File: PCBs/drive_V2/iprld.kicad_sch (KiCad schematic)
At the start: 81 parts, among them IC1 W25Q16JVUXIQ_TR, IC2 ADS1115IDGSR, J1 TYPE-C-31-M-12, U1 AMS1117-3.3, U11 4N35, U12 4N35, U13 4N35, U14 4N35, U2 ESP32-S3, U3 4N35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

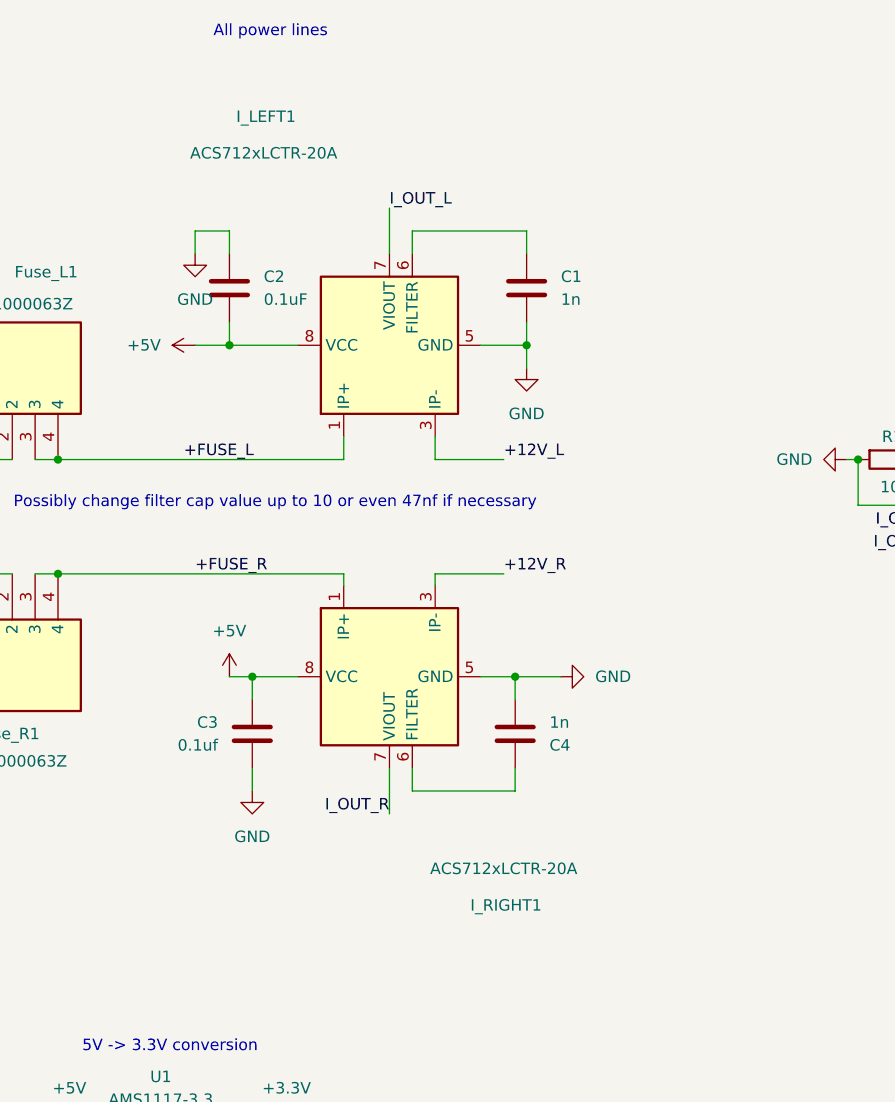
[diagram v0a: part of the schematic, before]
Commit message: added potential divider for I_OUT signals
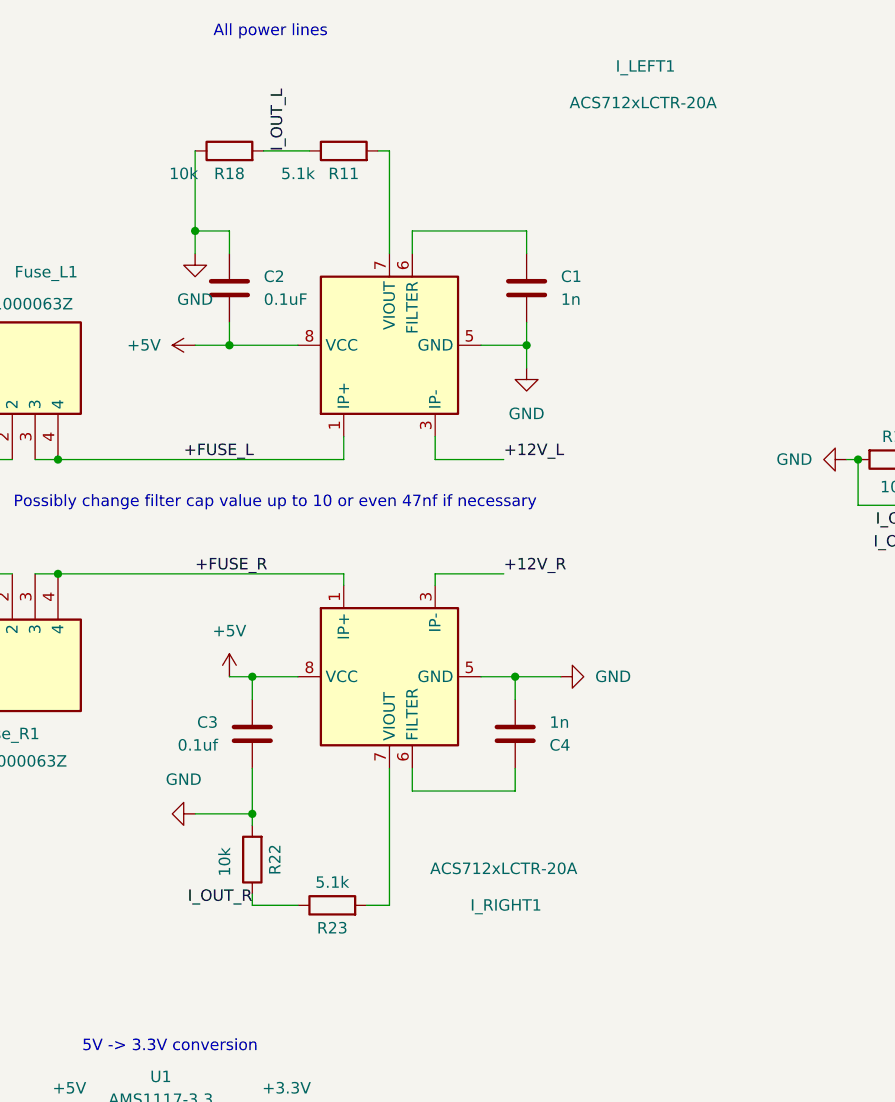
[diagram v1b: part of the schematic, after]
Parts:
- added R11, R23: 5.1k, Resistor_SMD:R_0805_2012Metric, symbol Device:R
- added R18, R22: 10k, Resistor_SMD:R_0805_2012Metric, symbol Device:R
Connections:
- net GND: now also R18.1, R22.2
- net I_OUT_L: now also R11.1, R18.2; no longer I_LEFT1.7 (VIOUT)
- net I_OUT_R: now also R22.1, R23.1; no longer I_RIGHT1.7 (VIOUT)
- new net: I_LEFT1.7 (VIOUT), R11.2
- new net: I_RIGHT1.7 (VIOUT), R23.2

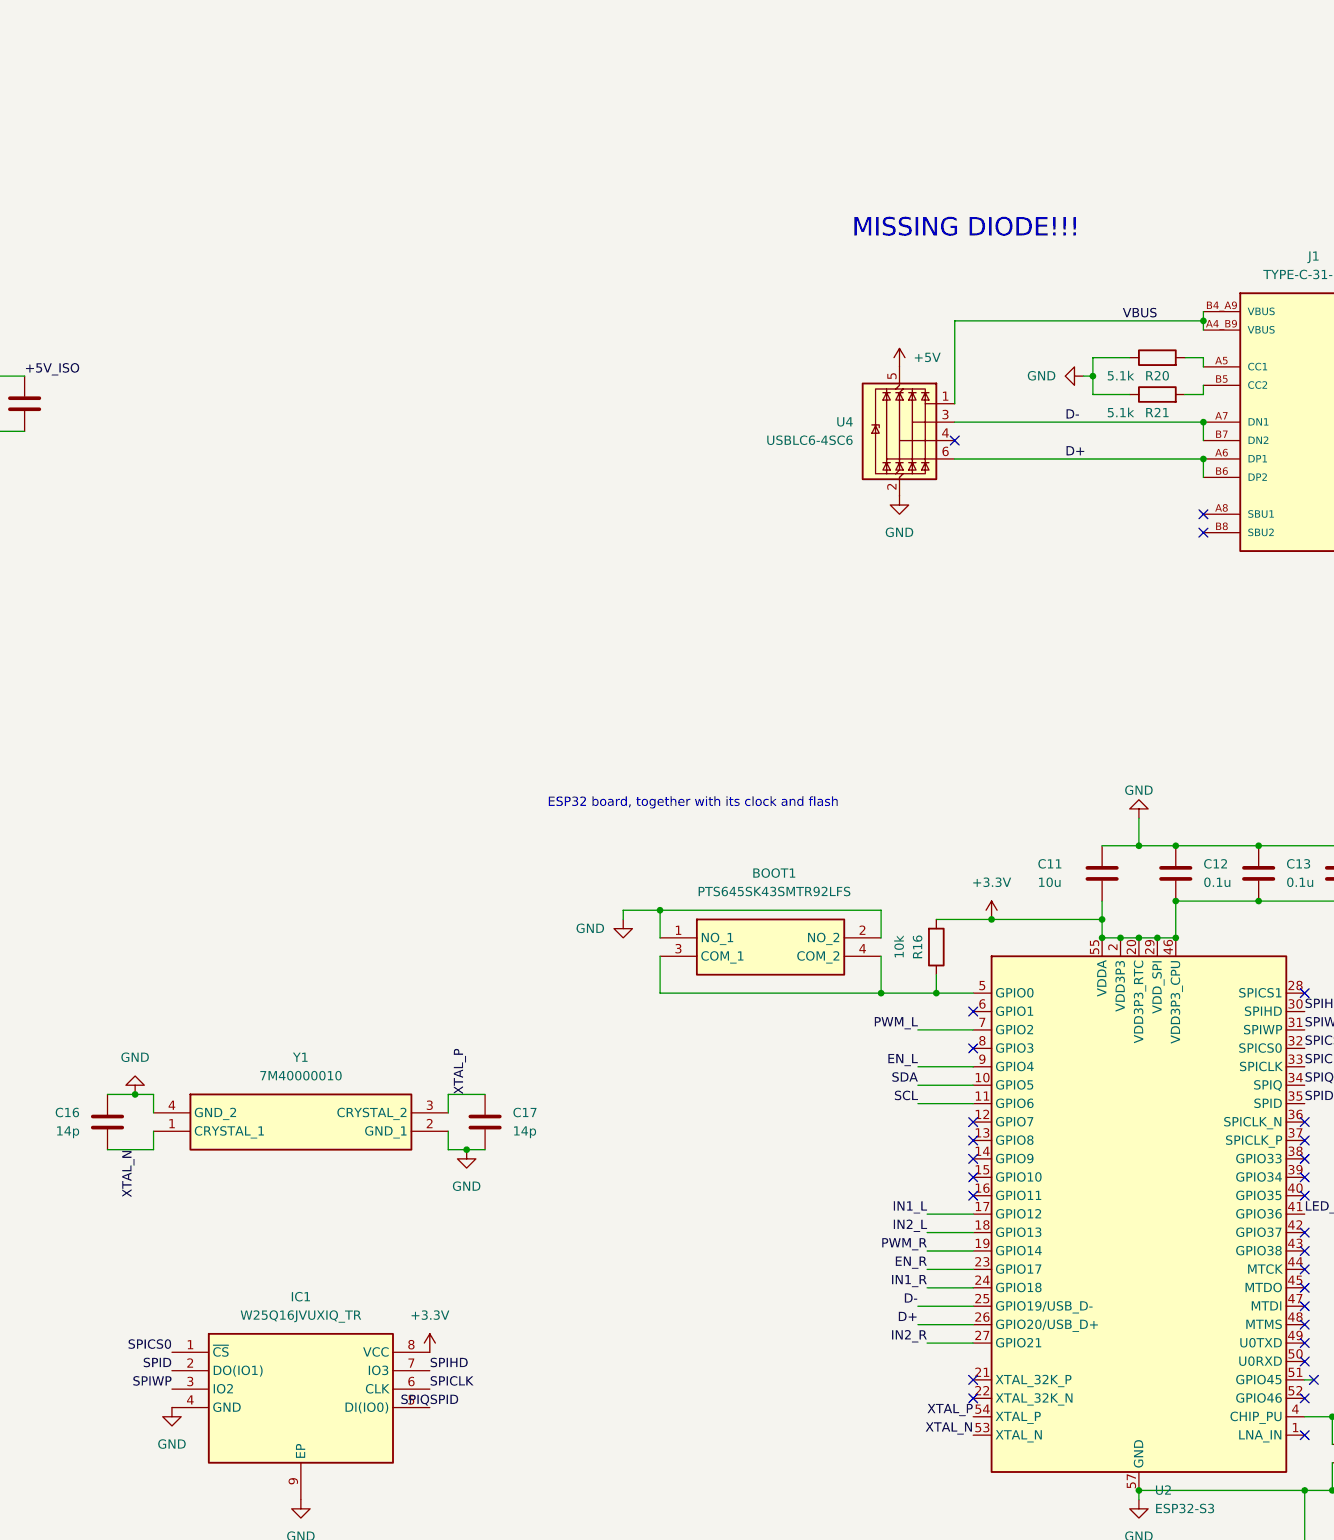
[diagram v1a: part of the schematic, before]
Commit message: readded Diode D1, fixed connection issue with SPID and SPIQ
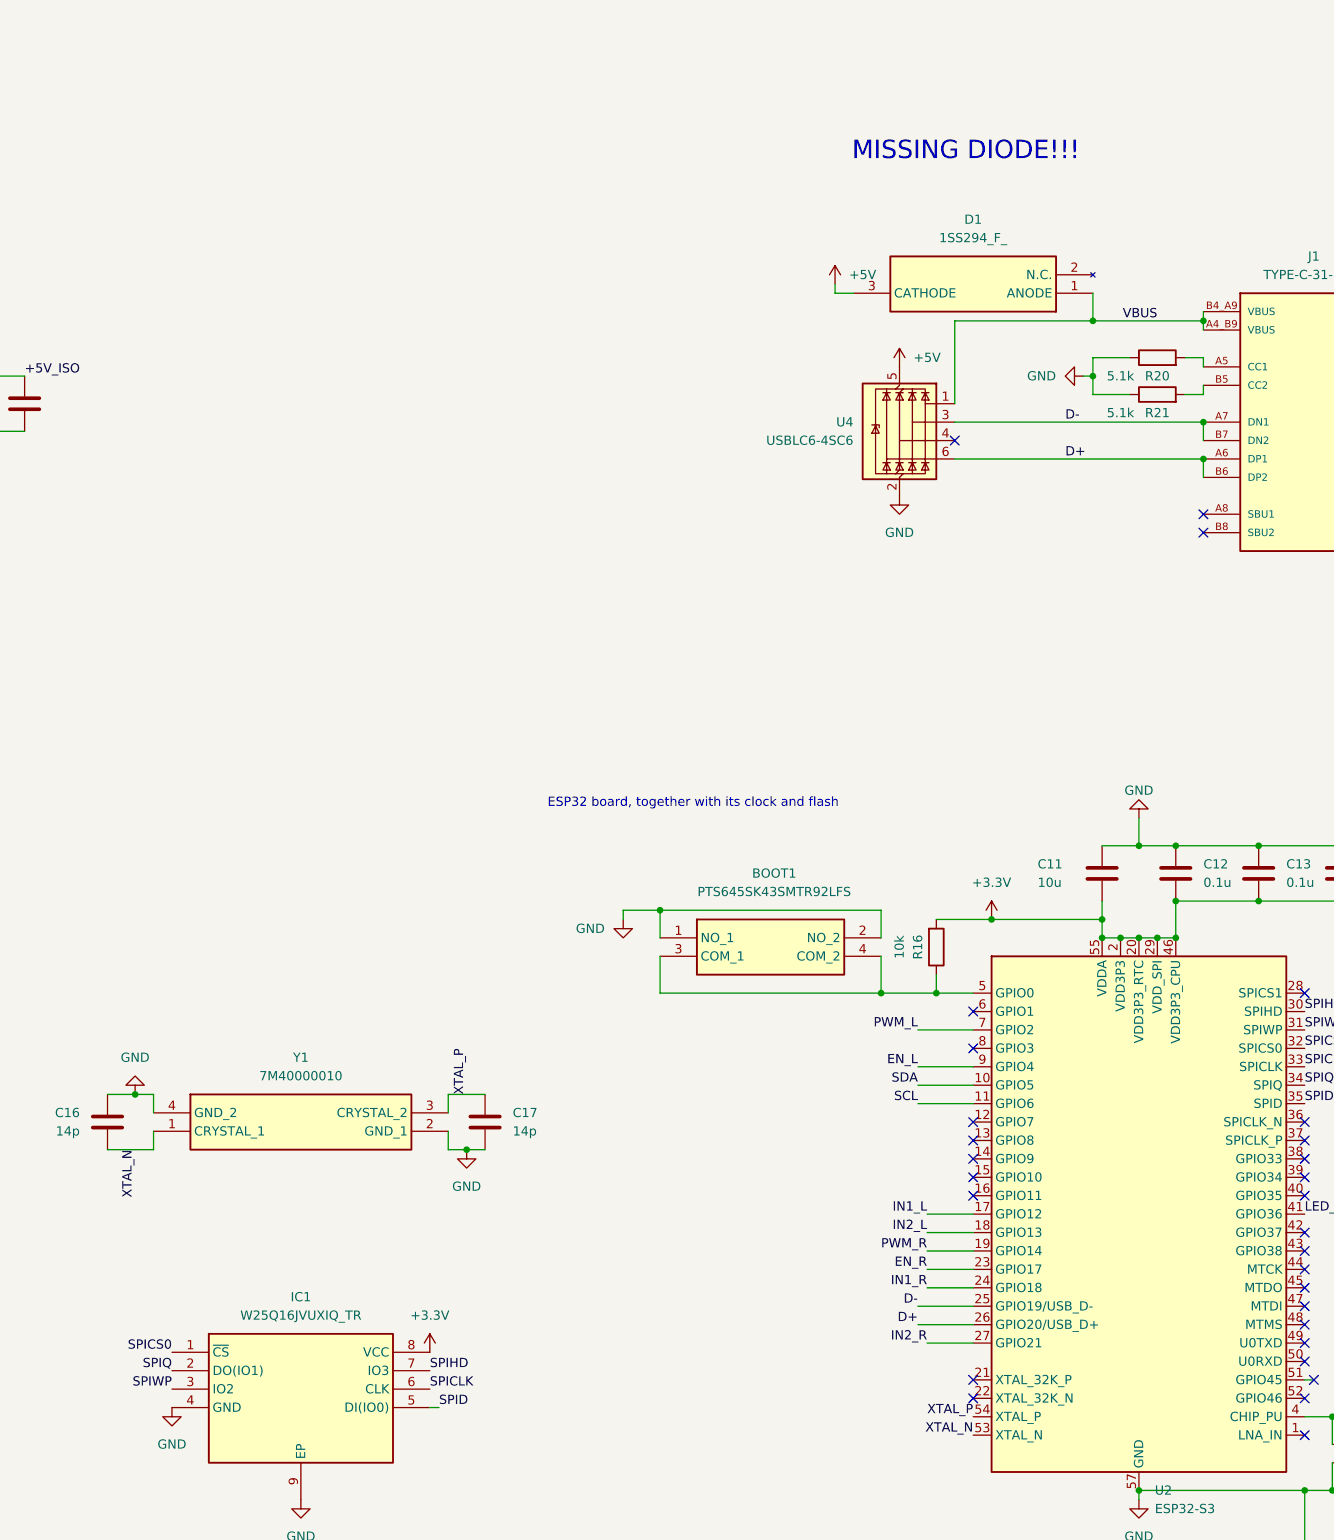
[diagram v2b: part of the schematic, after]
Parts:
- added D1: 1SS294_F_, iprl_footprint:SOT95P260X140-3N, symbol 1SS294_F_:1SS294_F_
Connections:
- net +5V: now also D1.3 (CATHODE)
- net SPID: no longer IC1.2 (DO(IO1)), U2.34 (SPIQ)
- net VBUS: now also D1.1 (ANODE)
- new net SPIQ: IC1.2 (DO(IO1)), U2.34 (SPIQ)

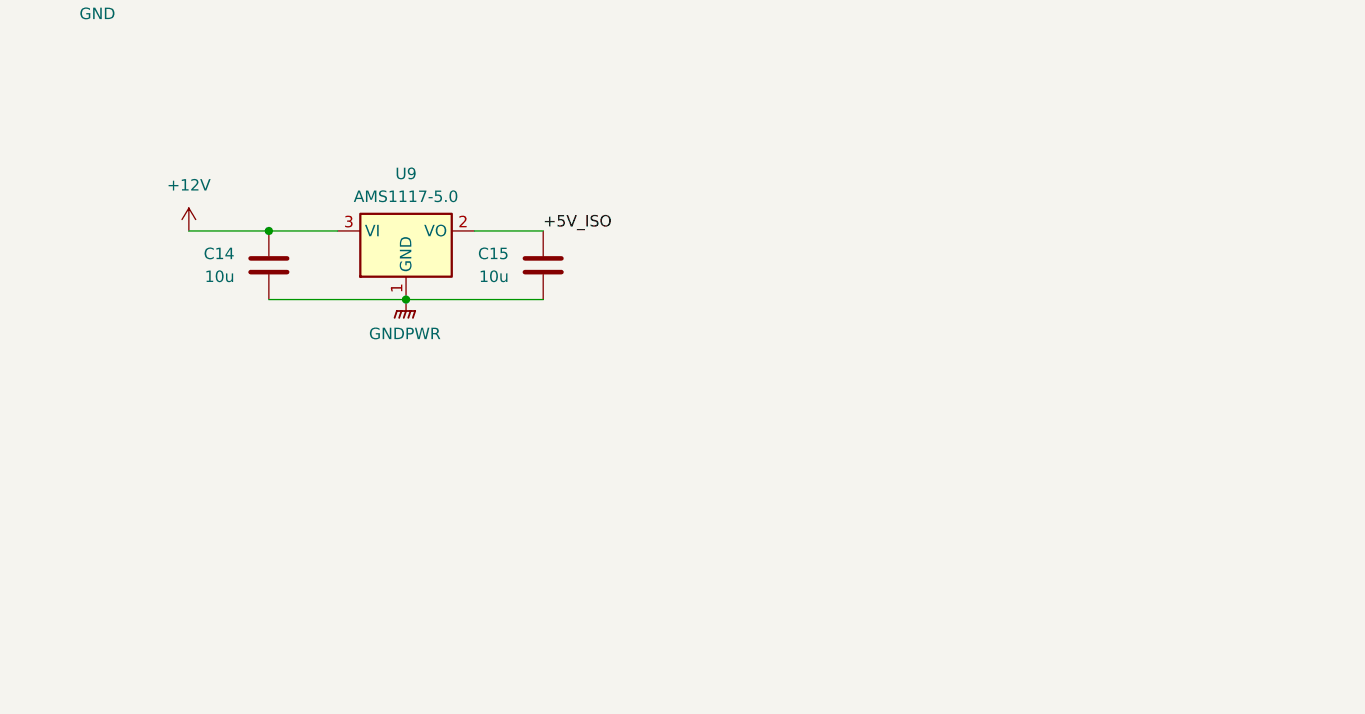
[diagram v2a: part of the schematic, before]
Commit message: Switched the LDO to LM317
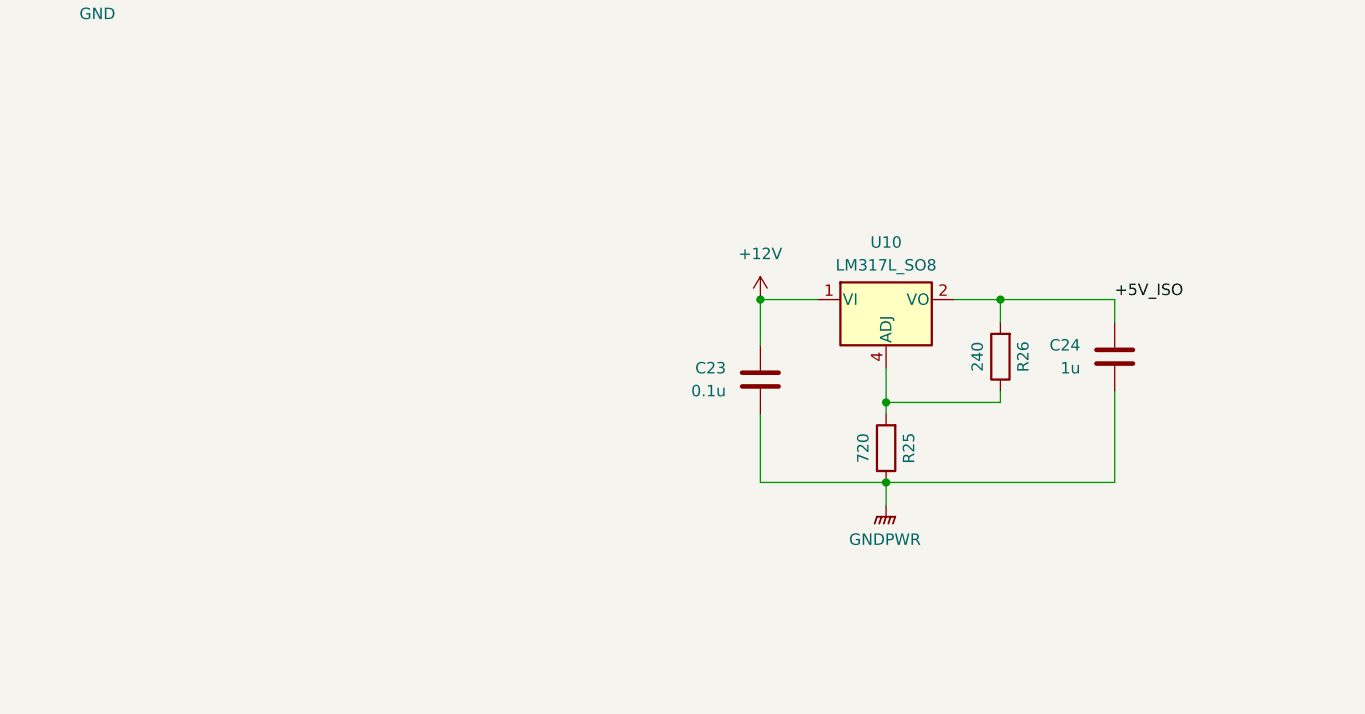
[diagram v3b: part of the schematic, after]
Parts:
- removed C14, C15: 10u, Capacitor_SMD:C_0603_1608Metric, symbol Device:C
- removed U9: AMS1117-5.0, Package_TO_SOT_SMD:SOT-223-3_TabPin2, symbol Regulator_Linear:AMS1117-5.0
- added C23: 0.1u, Capacitor_SMD:C_0603_1608Metric, symbol Device:C
- added C24: 1u, Capacitor_SMD:C_0603_1608Metric, symbol Device:C
- added R25: 720, Resistor_SMD:R_0805_2012Metric, symbol Device:R
- added R26: 240, Resistor_SMD:R_0805_2012Metric, symbol Device:R
- added U10: LM317L_SO8, Package_SO:SOIC-8_3.9x4.9mm_P1.27mm, symbol Regulator_Linear:LM317L_SO8
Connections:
- net +12V: now also C23.1, U10.1 (VI)
- net +5V_ISO: now also C24.1, R26.2, U10.2 (VO), U10.3 (VO), U10.6 (VO), U10.7 (VO)
- net GNDPWR: now also C23.2, C24.2, R25.1
- new net: R25.2, R26.1, U10.4 (ADJ)
